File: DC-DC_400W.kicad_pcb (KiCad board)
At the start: 2 copper layers, 96 x 63 mm, 6 parts, among them J1 Conn_01x24, J2 Conn_01x03, J3 Conn_01x10, J4 Conn_01x10, J6 Conn_01x02

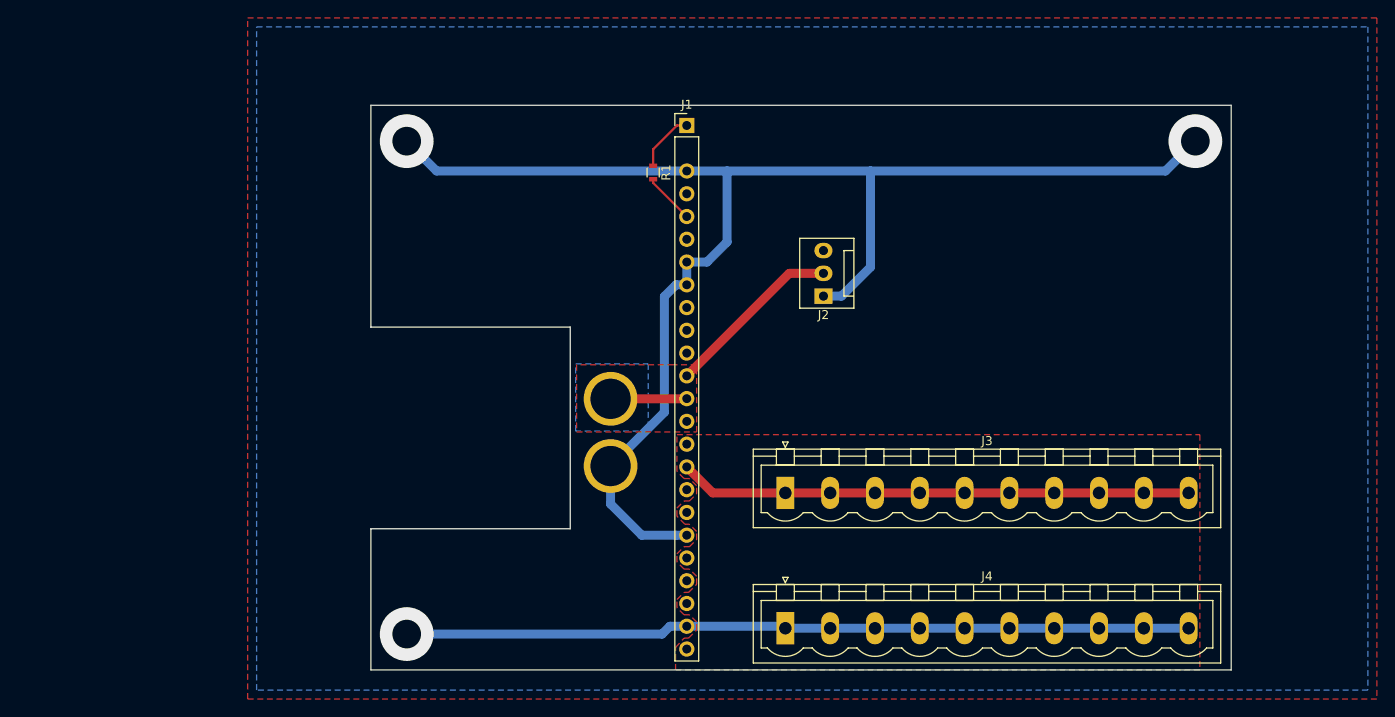
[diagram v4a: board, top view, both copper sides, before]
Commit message: gerber generated + pcb fixes
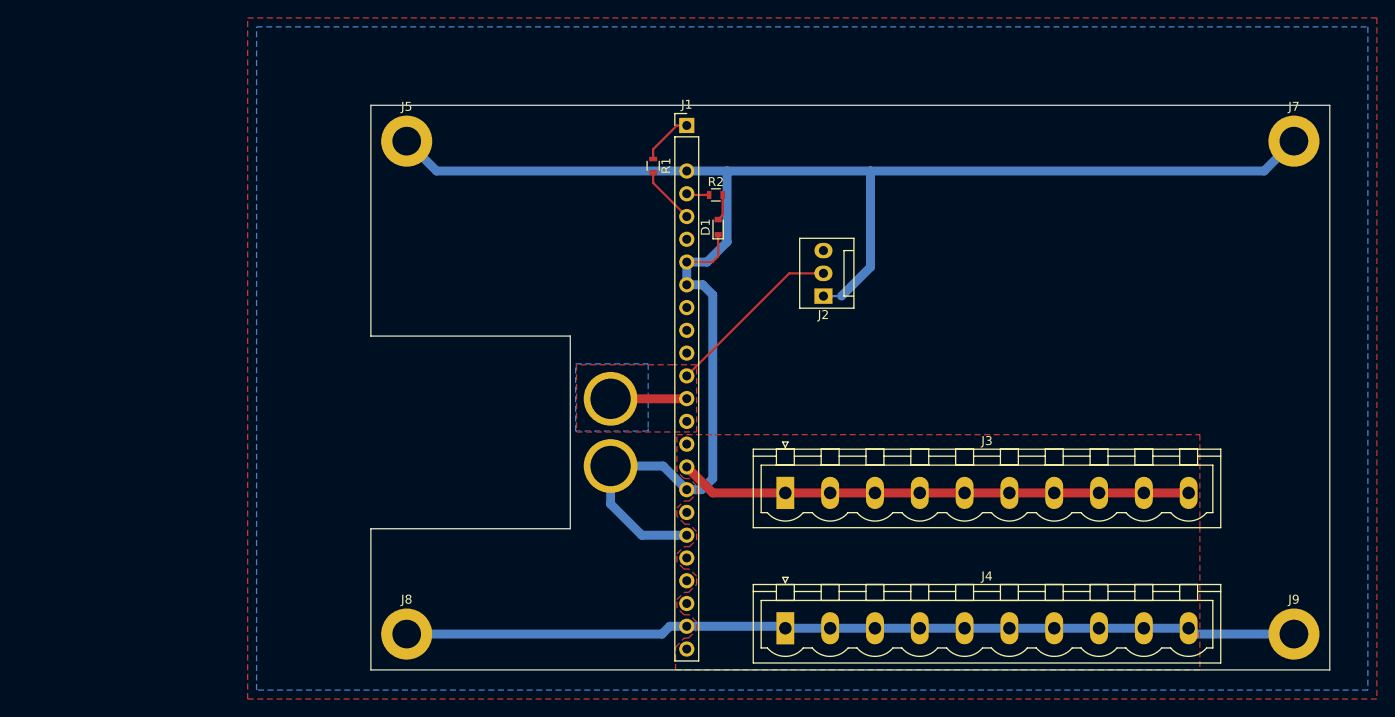
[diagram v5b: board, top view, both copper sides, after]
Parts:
- added D1: LED, Diodes_SMD:D_0603, F.Cu at (129.5, 80.3)
- added J5: Conn_01x01, Mounting_Holes:MountingHole_3.2mm_M3_ISO7380_Pad, F.Cu at (94.8, 70.8)
- added J7: Conn_01x01, Mounting_Holes:MountingHole_3.2mm_M3_ISO7380_Pad, F.Cu at (193.8, 70.8)
- added J8: Conn_01x01, Mounting_Holes:MountingHole_3.2mm_M3_ISO7380_Pad, F.Cu at (94.8, 125.8)
- added J9: Conn_01x01, Mounting_Holes:MountingHole_3.2mm_M3_ISO7380_Pad, F.Cu at (193.8, 125.8)
- added R2: 680R, Resistors_SMD:R_0603, F.Cu at (129.2, 76.8)
- moved R1 0.75 mm to (122.2, 73.5)
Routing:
- net GND: track 250.3 -> 291.9 mm, vias 3 -> 0
- net Net-(D1-Pad2): track 0.00 -> 2.96 mm
- net /PWR_GOOD: track 0.00 -> 2.55 mm
- net /TRIM-: track 5.71 -> 6.46 mm
- net /TRIM+: track 6.70 -> 5.95 mm
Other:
- board size 96 x 63 mm -> 107 x 63 mm

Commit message: almost done
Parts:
- removed J4: Conn_01x10, Connectors_Phoenix:PhoenixContact_MSTBVA-G_10x5.00mm_Vertical
- added J10: Conn_01x05, Connectors_Phoenix:PhoenixContact_MSTBVA-G_05x5.00mm_Vertical, F.Cu at (135.1, 112.0)
- J3: value Conn_01x10 -> Conn_01x05; footprint Connectors_Phoenix:PhoenixContact_MSTBVA-G_10x5.00mm_Vertical -> Connectors_Phoenix:PhoenixContact_MSTBVA-G_05x5.00mm_Vertical
- moved J7 30.0 mm to (163.8, 70.8)
- moved J9 30.0 mm to (163.8, 125.8)
- moved J3 14.2 mm to (135.1, 124.1)
- moved D1 3.41 mm to (132.9, 80.2)
- moved R2 2.90 mm to (132.2, 76.8)
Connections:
- J3 pad 1: +5V -> GND
- J3 pad 2: +5V -> GND
- J3 pad 3: +5V -> GND
- J3 pad 4: +5V -> GND
- J3 pad 5: +5V -> GND
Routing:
- net GND: track 291.9 -> 224.1 mm, vias 0 -> 75
- net +5V: track 57.2 -> 0.00 mm
- net +12V: track 28.5 -> 36.6 mm, vias 0 -> 4
- net /PWR_GOOD: track 2.55 -> 5.45 mm
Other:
- board size 107 x 63 mm -> 77 x 63 mm
- rule trace_min: 0.2 -> 0.25
